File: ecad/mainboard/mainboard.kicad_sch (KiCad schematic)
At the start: 45 parts, among them J2 LCD Display Header, J3 Conn_01x06_Socket, J4 TYPE-C-31-M-12, Q1 MMBT2222A, SW1 SW_MEC_5E, SW2 SW_MEC_5E, SW3 SW_MEC_5E, SW4 SW_MEC_5E, U1 PCF8574T, U2 CH340E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

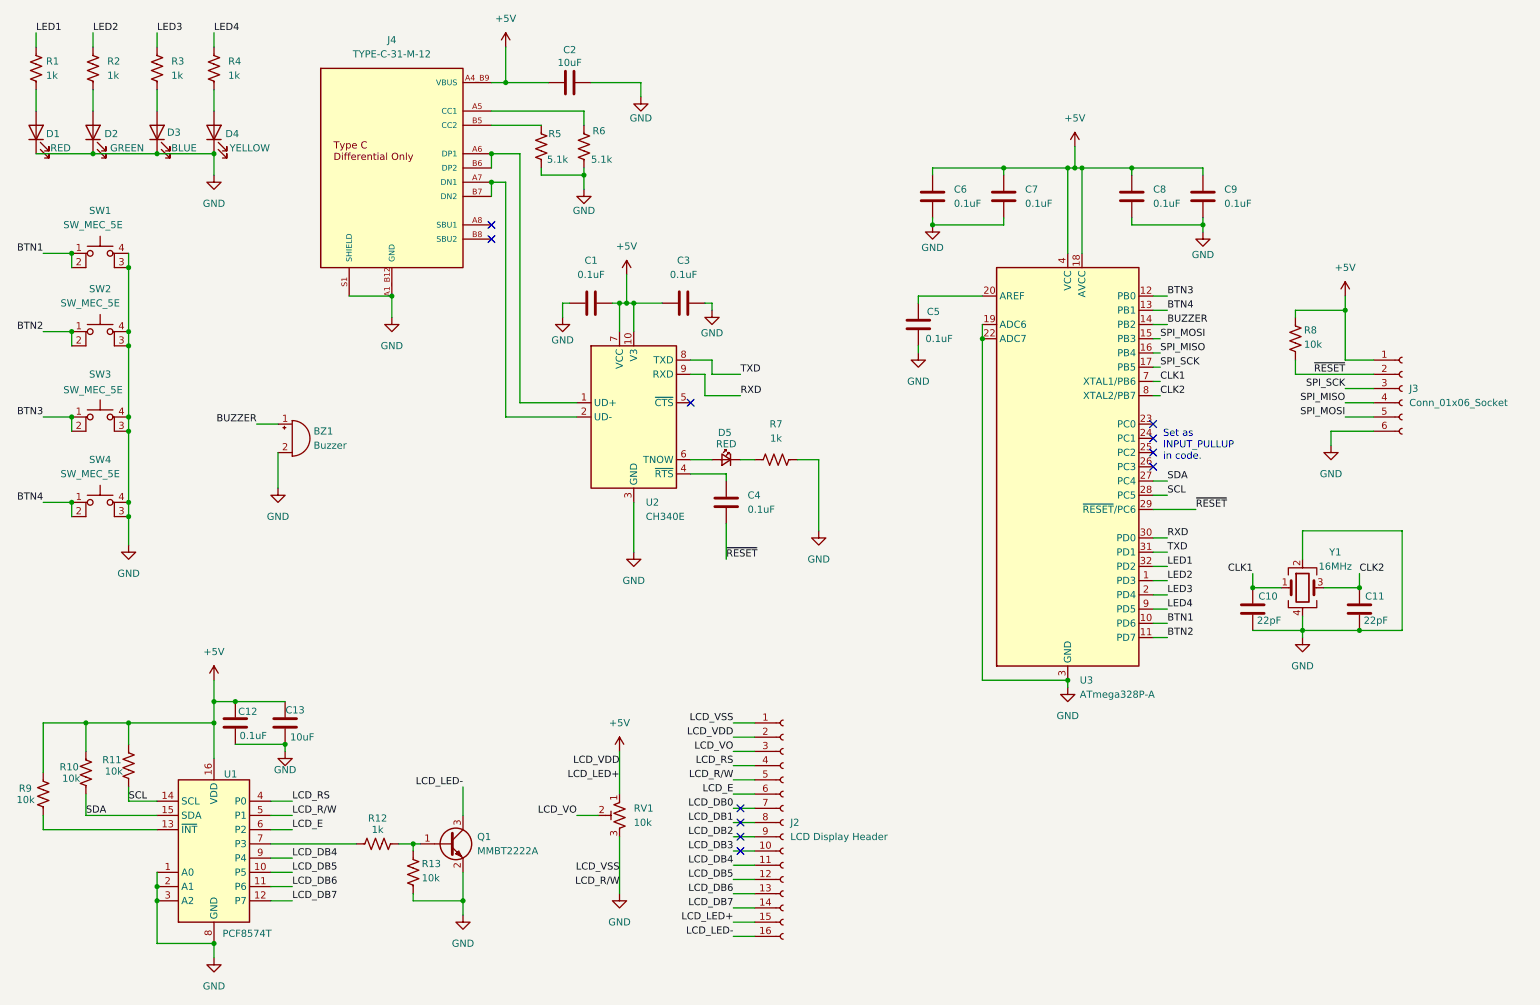
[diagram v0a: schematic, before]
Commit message: add led sub schematic to manage led outputs
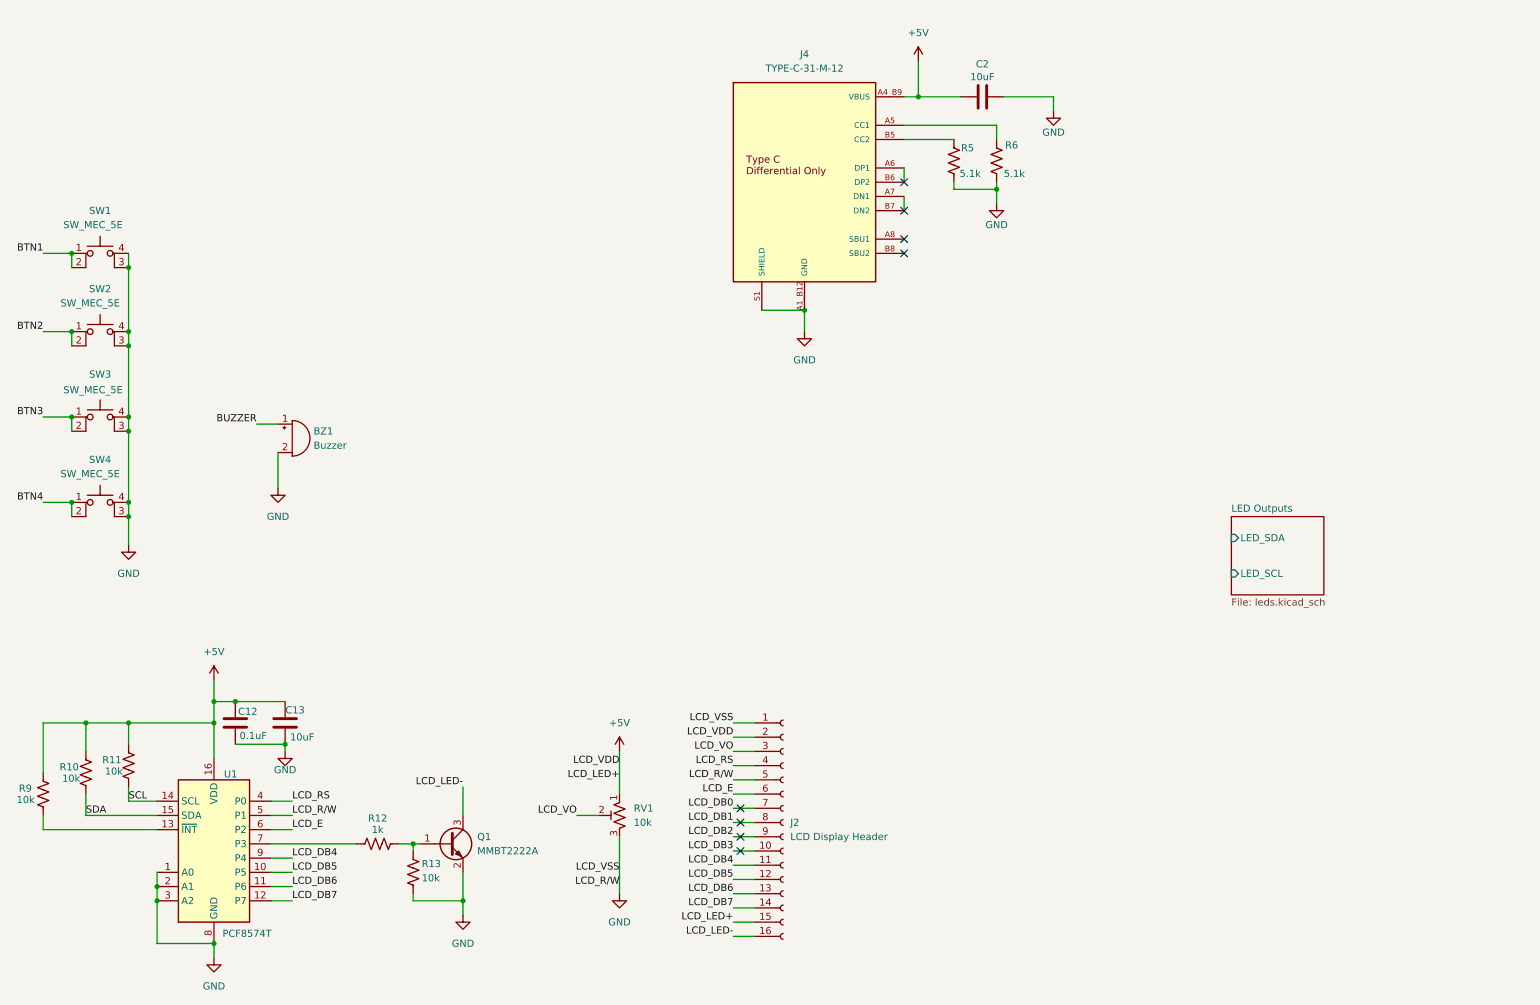
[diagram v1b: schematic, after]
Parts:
- removed C1, C3, C4, C5, C6, C7, C8, C9: 0.1uF, Capacitor_SMD:C_0603_1608Metric, symbol Device:C
- removed C10, C11: 22pF, Capacitor_SMD:C_0402_1005Metric, symbol Device:C
- removed D1: RED, LED_SMD:LED_0603_1608Metric, symbol Device:LED
- removed D2: GREEN, LED_SMD:LED_0603_1608Metric, symbol Device:LED
- removed D3: BLUE, LED_SMD:LED_0603_1608Metric, symbol Device:LED
- removed D4: YELLOW, LED_SMD:LED_0603_1608Metric, symbol Device:LED
- removed D5: RED, LED_SMD:LED_0402_1005Metric, symbol Device:LED_Small
- removed J3: Conn_01x06_Socket, Connector_PinSocket_2.54mm:PinSocket_1x06_P2.54mm_Vertical, symbol Connector:Conn_01x06_Socket
- removed R1, R2, R3, R4, R7: 1k, Resistor_SMD:R_0603_1608Metric, symbol Device:R_US
- removed R8: 10k, Resistor_SMD:R_0603_1608Metric, symbol Device:R_US
- removed U2: CH340E, Package_SO:MSOP-10_3x3mm_P0.5mm, symbol Interface_USB:CH340E
- removed U3: ATmega328P-A, Package_QFP:TQFP-32_7x7mm_P0.8mm, symbol MCU_Microchip_ATmega:ATmega328P-A
- removed Y1: 16MHz, Crystal:Crystal_SMD_SeikoEpson_TSX3225-4Pin_3.2x2.5mm, symbol Device:Crystal_GND24
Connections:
- no-connect marks 11 -> 8
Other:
- added sheet LED Outputs (leds.kicad_sch)
- note removed: "Set as INPUT_PULLUP in code."
- moved on the sheet: C2, J4, R5, R6
